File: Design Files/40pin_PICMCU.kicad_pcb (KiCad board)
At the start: 2 copper layers, 25.4 x 62.9 mm, 29 parts, among them CON1 USB-MICRO-B, P1 CONN_10, P10 CONN_01X01, P2 CONN_10, P3 CONN_10, P4 CONN_10, P5 CONN_01X01, P6 ICSP, P7 CONN_01X01, P8 CONN_01X01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

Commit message: Changes Done
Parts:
- CON1: footprint EE:USB_Micro-B_SMD_NEW -> Explore:USB_Micro-B_SMD_NEW_1
- D1, D3: footprint EE:LED-0603_NEW -> Explore:LED-0603_NEW
- JP1: footprint Pin_Headers:Pin_Header_Straight_1x02 -> Pin_Headers:Pin_Header_Straight_1x02_Pitch2.54mm
- P1, P2, P3, P4: footprint Pin_Headers:Pin_Header_Straight_1x10 -> Pin_Headers:Pin_Header_Straight_1x10_Pitch2.54mm
- P6: footprint Pin_Headers:Pin_Header_Straight_1x06 -> Pin_Headers:Pin_Header_Straight_1x06_Pitch2.54mm
- P7: footprint Logo_new:Logo_8 -> E_Logo:Logo_8
- SW1: footprint EE:SW_PUSH_SMALL_2pin_3D_xl -> Explore:SW_PUSH_SMALL_2pin_3D_xl_v1
- U1: footprint EE:cp2102_xl2 -> Explore:cp2102_xl2
- X1: footprint Crystals:HC-49V -> Crystals:Crystal_HC18-U_Vertical
- moved P7 16.4 mm to (140.6, 96.1)
- moved CON1 1.52 mm to (139.7, 89.3)
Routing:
- net Net-(CON1-Pad2): track 6.53 -> 12.0 mm
- net Net-(CON1-Pad3): track 5.15 -> 7.08 mm
- net /+5V: track 134.9 -> 136.5 mm
- net GND: track 141.4 -> 142.9 mm
- net /RX: track 108.5 -> 107.0 mm
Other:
- outline, holes or cut-outs redrawn
- board text added: "oneMicro"
- board text removed: "PWR"

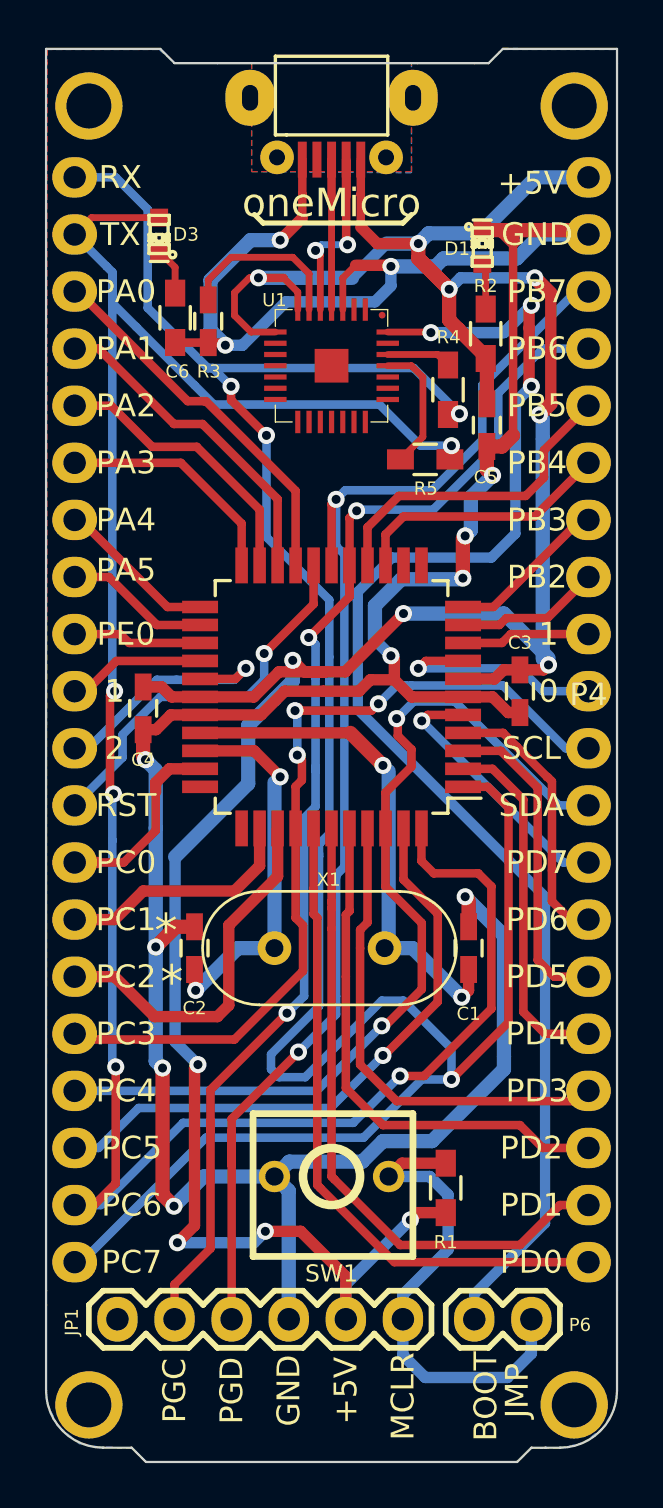
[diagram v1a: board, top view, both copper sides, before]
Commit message: Added Reset connectin
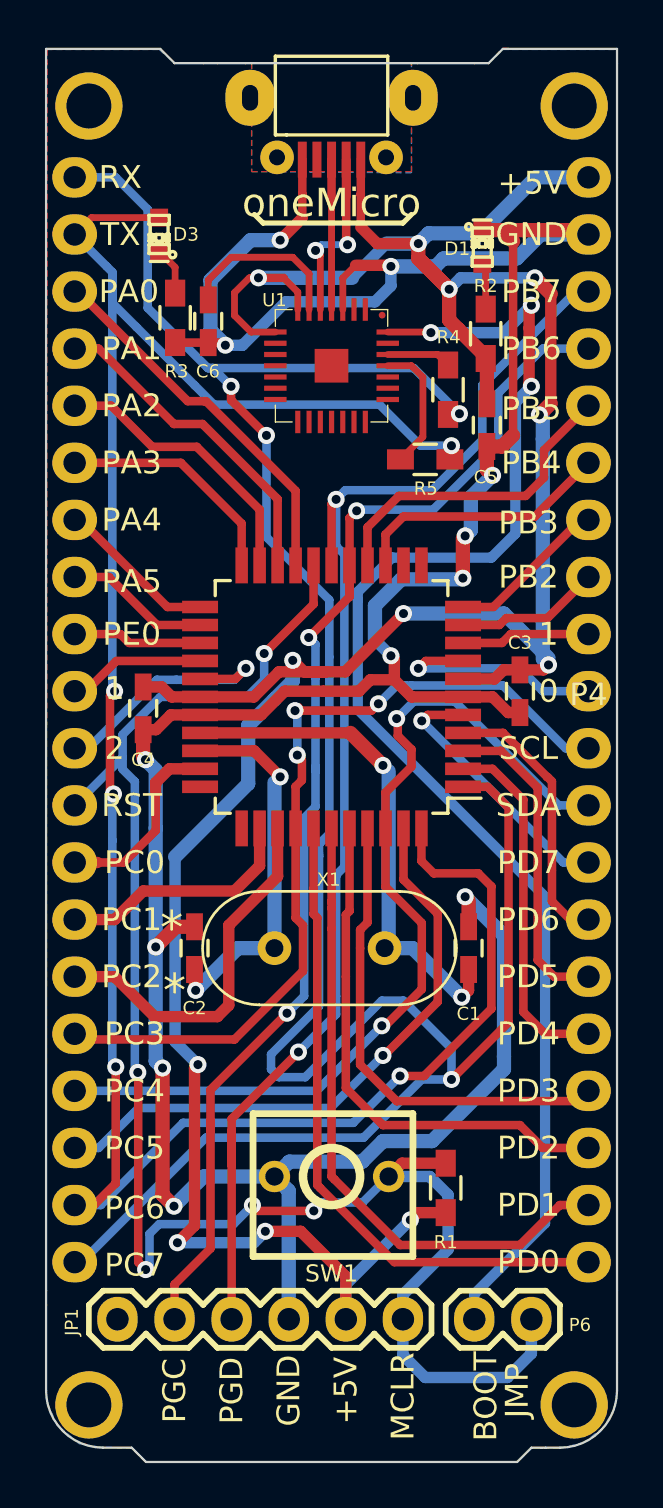
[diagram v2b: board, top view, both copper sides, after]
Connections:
- P1 pad 9: /RST -> /MCLR
- U***1 pad 18: /RST -> /MCLR
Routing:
- net /MCLR: track 21.8 -> 75.9 mm, vias 0 -> 5
- net /RST: track 17.3 -> 0.00 mm, vias 1 -> 0

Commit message: Revised gerber file generated for v1.0
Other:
- board text added: "v1.0"
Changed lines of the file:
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@@
-(kicad_pcb (version 4) (host pcbnew 4.0.5)
+(kicad_pcb (version 4) (host pcbnew 4.0.4-stable)
   (general
     (links 84)
@@
     (area 126.949999 84.404999 152.450001 147.370001)
     (thickness 1.6)
-    (drawings 94)
+    (drawings 95)
     (tracks 643)
     (zones 0)
@@
   )
   (setup
-    (last_trace_width 0.381)
+    (last_trace_width 0.254)
     (user_trace_width 0.3048)
     (user_trace_width 0.381)
@@
     (visible_elements 7FFEFFFF)
     (pcbplotparams
-      (layerselection 0x00030_80000001)
+      (layerselection 0x000f0_80000001)
       (usegerberextensions true)
-      (excludeedgelayer true)
+      (excludeedgelayer false)
       (linewidth 0.150000)
       (plotframeref false)
@@
       (drillshape 0)
       (scaleselection 1)
-      (outputdirectory ""))
+      (outputdirectory "Gerber Data/"))
   )
   (net 0 "")
@@
     )
   )
+  (gr_text v1.0 (at 139.68984 86.80704) (layer B.SilkS)
+    (effects (font (size 1.5 1.5) (thickness 0.3)) (justify mirror))
+  )
   (gr_line (start 131.699 94.107) (end 131.318 93.726) (angle 90) (layer B.SilkS) (width 0.2286))
